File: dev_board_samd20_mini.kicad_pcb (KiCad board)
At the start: 2 copper layers, 34.9 x 34.3 mm, 9 parts, among them J1 Conn_02x05_Odd_Even, J2 Conn_02x08, J3 Conn_01x10, J4 Conn_02x08, U1 SAMD20G18A-AU

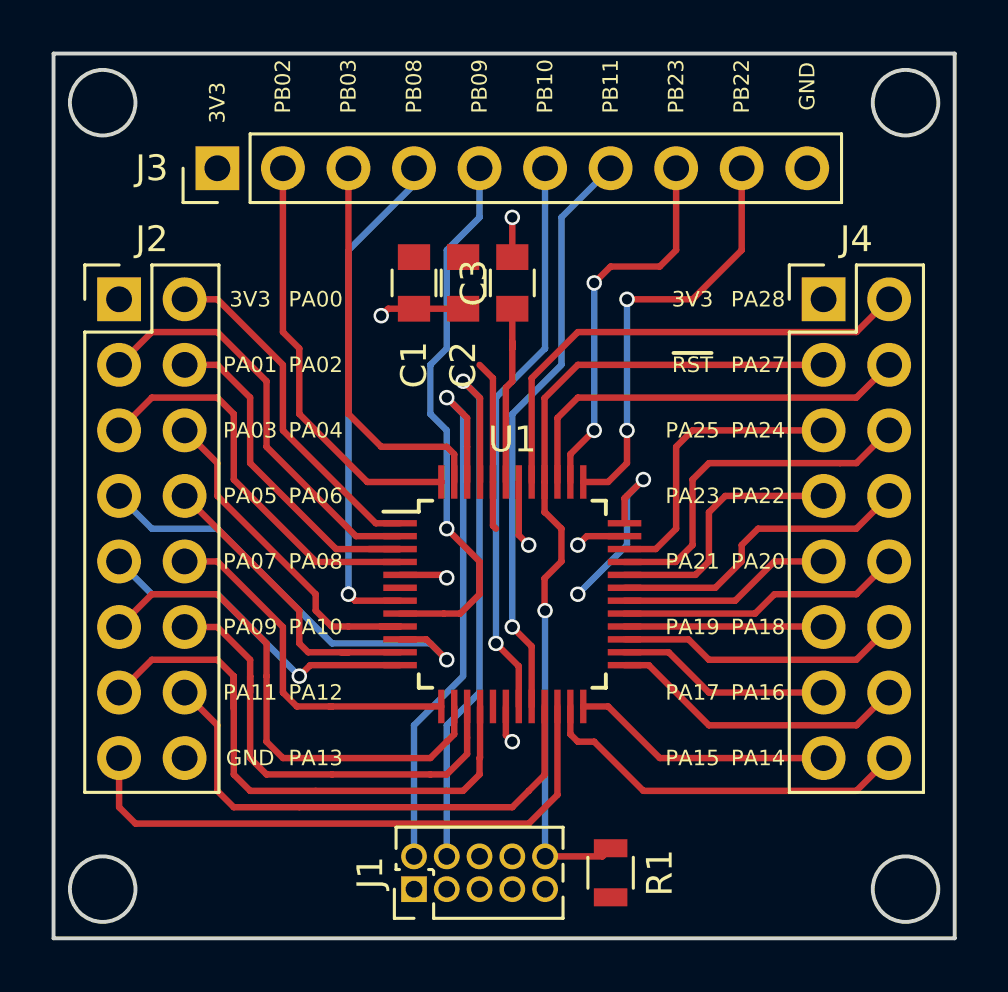
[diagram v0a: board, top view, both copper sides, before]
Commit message: Réduction de la taille de la carte
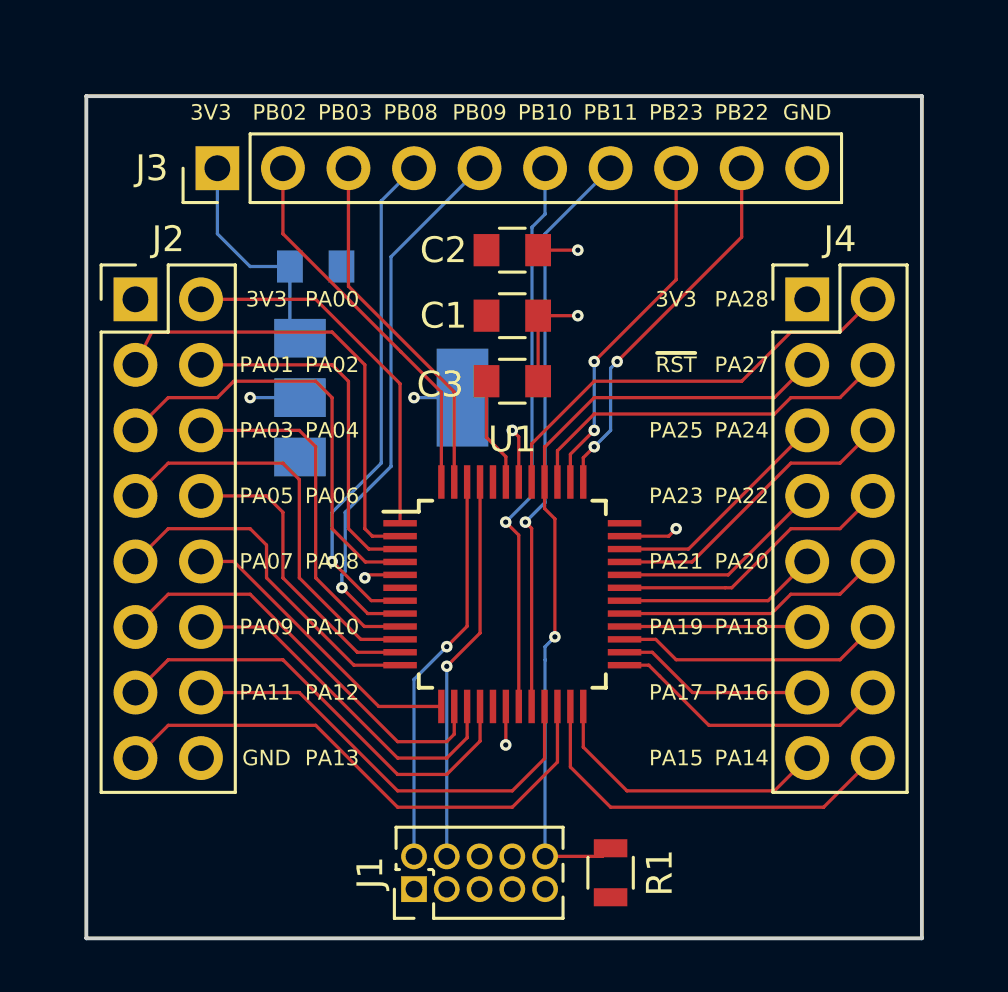
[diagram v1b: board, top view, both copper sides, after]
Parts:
- added C4: 10uF, Capacitors_SMD:C_0805, B.Cu at (138.4, 95.2)
- added U2: LM1117-3.3, TO_SOT_Packages_SMD:SOT-223, B.Cu at (141.0, 100.3)
- moved C1 4.02 mm to (146.1, 97.2), turned to 0 degrees
- moved C3 3.81 mm to (146.1, 99.7), turned to 0 degrees
- moved C2 2.29 mm to (146.1, 94.6), turned to 0 degrees
- moved J4 0.64 mm to (157.5, 96.5)
- moved J2 0.63 mm to (131.4, 96.5)
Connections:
- J3 pad 1: +3V3 -> VDD
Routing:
- net +3V3: track 14.2 -> 3.81 mm
- net VDD: track 0.00 -> 8.82 mm
- net /SWCLK: track 23.4 -> 15.0 mm
- net /SWDIO: track 22.4 -> 15.4 mm
- net /PA11: track 23.0 -> 17.6 mm
- net /PA10: track 18.4 -> 14.0 mm
- net /PA9: track 19.8 -> 16.4 mm
- net /PA12: track 20.5 -> 17.4 mm
- net Net-(C3-Pad1): track 7.09 -> 4.22 mm
- net /PA25: track 11.5 -> 8.99 mm
- net /PA8: track 13.9 -> 11.6 mm
- net /PA24: track 13.9 -> 11.7 mm
- net /PA28: track 19.1 -> 17.0 mm
- net /PB22: track 16.8 -> 14.7 mm
- net /PA13: track 23.0 -> 21.1 mm
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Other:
- board size 34.9 x 34.3 mm -> 32.4 x 32.6 mm
- net class Default: clearance 0.2 -> 0.1; trace_width 0.25 -> 0.127; via_dia 0.6 -> 0.45; via_drill 0.4 -> 0.2
- rule trace_clearance: 0.2 -> 0.1
- rule trace_min: 0.2 -> 0.1
- rule via_min_drill: 0.3 -> 0.2
- rule via_min_size: 0.4 -> 0.45
